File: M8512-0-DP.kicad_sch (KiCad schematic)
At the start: 1 part, among them J1 KL10_6-bay_backplane_connector

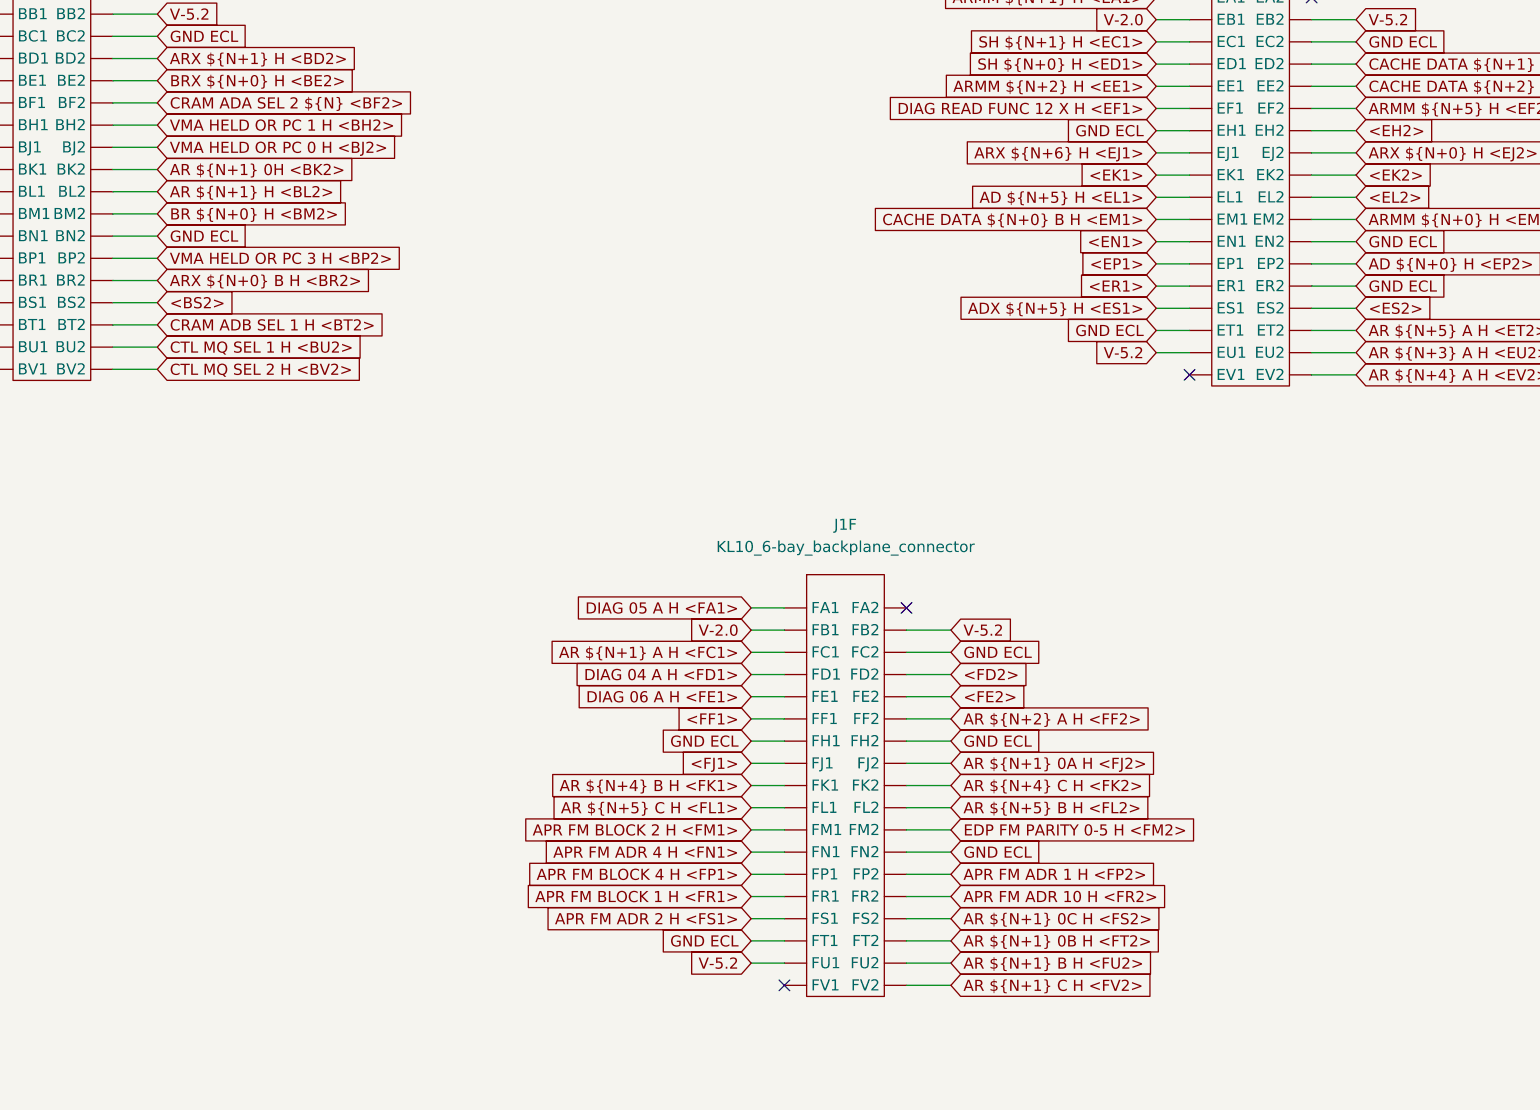
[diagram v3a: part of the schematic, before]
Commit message: Fix a few mislabeld backplane signal names - still more to do
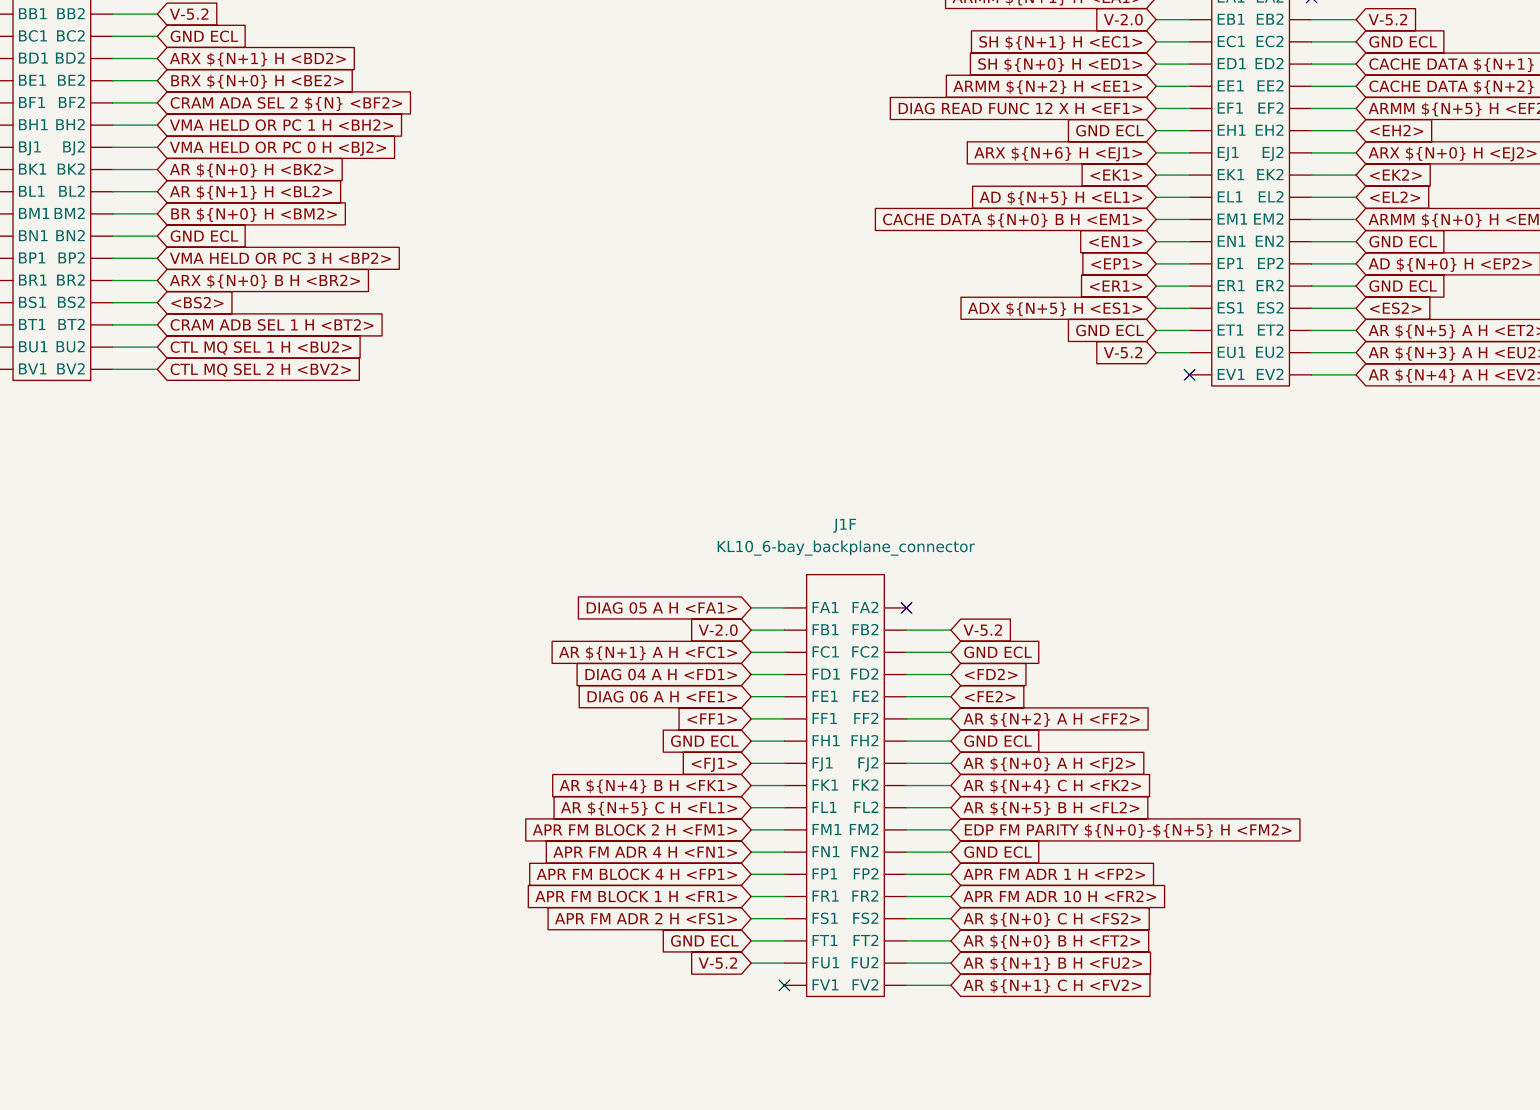
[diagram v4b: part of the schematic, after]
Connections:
- net AR ${N+1} 0A H <FJ2> renamed AR ${N+0} A H <FJ2>
- net AR ${N+1} 0B H <FT2> renamed AR ${N+0} B H <FT2>
- net AR ${N+1} 0C H <FS2> renamed AR ${N+0} C H <FS2>
- net AR ${N+1} 0H <BK2> renamed AR ${N+0} H <BK2>
- net EDP FM PARITY 0-5 H <FM2> renamed EDP FM PARITY ${N+0}-${N+5} H <FM2>
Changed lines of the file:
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@@
     )
   )
-  (global_label "AR ${N+1} 0H <BK2>" (shape input) (at 190.5 128.27 0) (fields_autoplaced)
-    (effects (font (size 1.27 1.27)) (justify left))
-    (property "Intersheet References" "${INTERSHEET_REFS}" (id 0) (at 207.6088 128.1906 0)
+  (global_label "AR ${N+0} H <BK2>" (shape input) (at 190.5 128.27 0) (fields_autoplaced)
+    (effects (font (size 1.27 1.27)) (justify left))
+    (property "Intersheet References" "${INTERSHEET_REFS}" (id 0) (at 213.4145 128.1906 0)
       (effects (font (size 1.27 1.27)) (justify left) hide)
     )
@@
     )
   )
-  (global_label "AR ${N+1} 0B H <FT2>" (shape input) (at 281.305 216.535 0) (fields_autoplaced)
-    (effects (font (size 1.27 1.27)) (justify left))
-    (property "Intersheet References" "${INTERSHEET_REFS}" (id 0) (at 300.1676 216.4556 0)
+  (global_label "AR ${N+0} B H <FT2>" (shape input) (at 281.305 216.535 0) (fields_autoplaced)
+    (effects (font (size 1.27 1.27)) (justify left))
+    (property "Intersheet References" "${INTERSHEET_REFS}" (id 0) (at 305.9733 216.4556 0)
       (effects (font (size 1.27 1.27)) (justify left) hide)
     )
@@
     )
   )
-  (global_label "AR ${N+1} 0C H <FS2>" (shape input) (at 281.305 213.995 0) (fields_autoplaced)
-    (effects (font (size 1.27 1.27)) (justify left))
-    (property "Intersheet References" "${INTERSHEET_REFS}" (id 0) (at 300.4095 213.9156 0)
+  (global_label "AR ${N+0} C H <FS2>" (shape input) (at 281.305 213.995 0) (fields_autoplaced)
+    (effects (font (size 1.27 1.27)) (justify left))
+    (property "Intersheet References" "${INTERSHEET_REFS}" (id 0) (at 306.2152 213.9156 0)
       (effects (font (size 1.27 1.27)) (justify left) hide)
     )
@@
     )
   )
-  (global_label "AR ${N+1} 0A H <FJ2>" (shape input) (at 281.305 196.215 0) (fields_autoplaced)
-    (effects (font (size 1.27 1.27)) (justify left))
-    (property "Intersheet References" "${INTERSHEET_REFS}" (id 0) (at 299.9862 196.1356 0)
+  (global_label "AR ${N+0} A H <FJ2>" (shape input) (at 281.305 196.215 0) (fields_autoplaced)
+    (effects (font (size 1.27 1.27)) (justify left))
+    (property "Intersheet References" "${INTERSHEET_REFS}" (id 0) (at 305.7919 196.1356 0)
       (effects (font (size 1.27 1.27)) (justify left) hide)
     )
@@
     )
   )
-  (global_label "EDP FM PARITY 0-5 H <FM2>" (shape input) (at 281.305 203.835 0) (fields_autoplaced)
-    (effects (font (size 1.27 1.27)) (justify left))
-    (property "Intersheet References" "${INTERSHEET_REFS}" (id 0) (at 313.291 203.7556 0)
-      (effects (font (size 1.27 1.27)) (justify left) hide)
-    )
+  (global_label "EDP FM PARITY ${N+0}-${N+5} H <FM2>" (shape input) (at 281.305 203.835 0) (fields_autoplaced)
+    (effects (font (size 1.27 1.27)) (justify left))
+    (property "Intersheet References" "${INTERSHEET_REFS}" (id 0) (at 324.9024 203.7556 0)
+      (effects (font (size 1.27 1.27)) (justify left) hide)
+    )

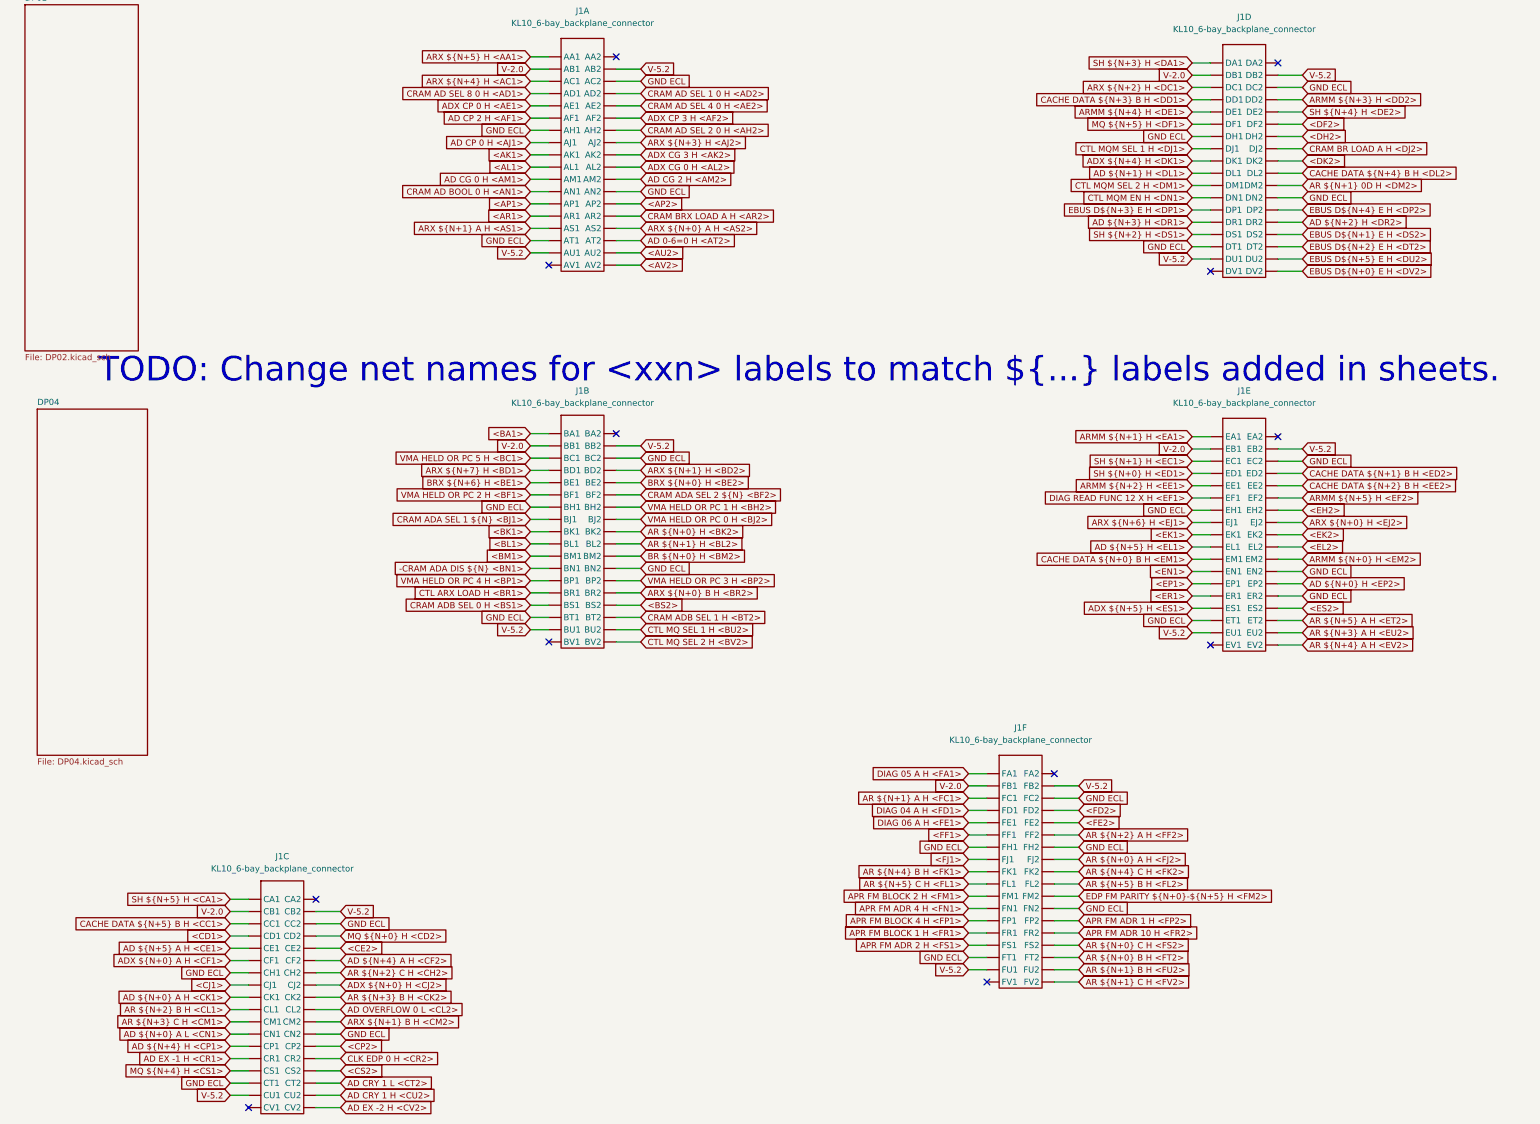
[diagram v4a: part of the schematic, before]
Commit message: Get rid of errors between J1 net name and pages
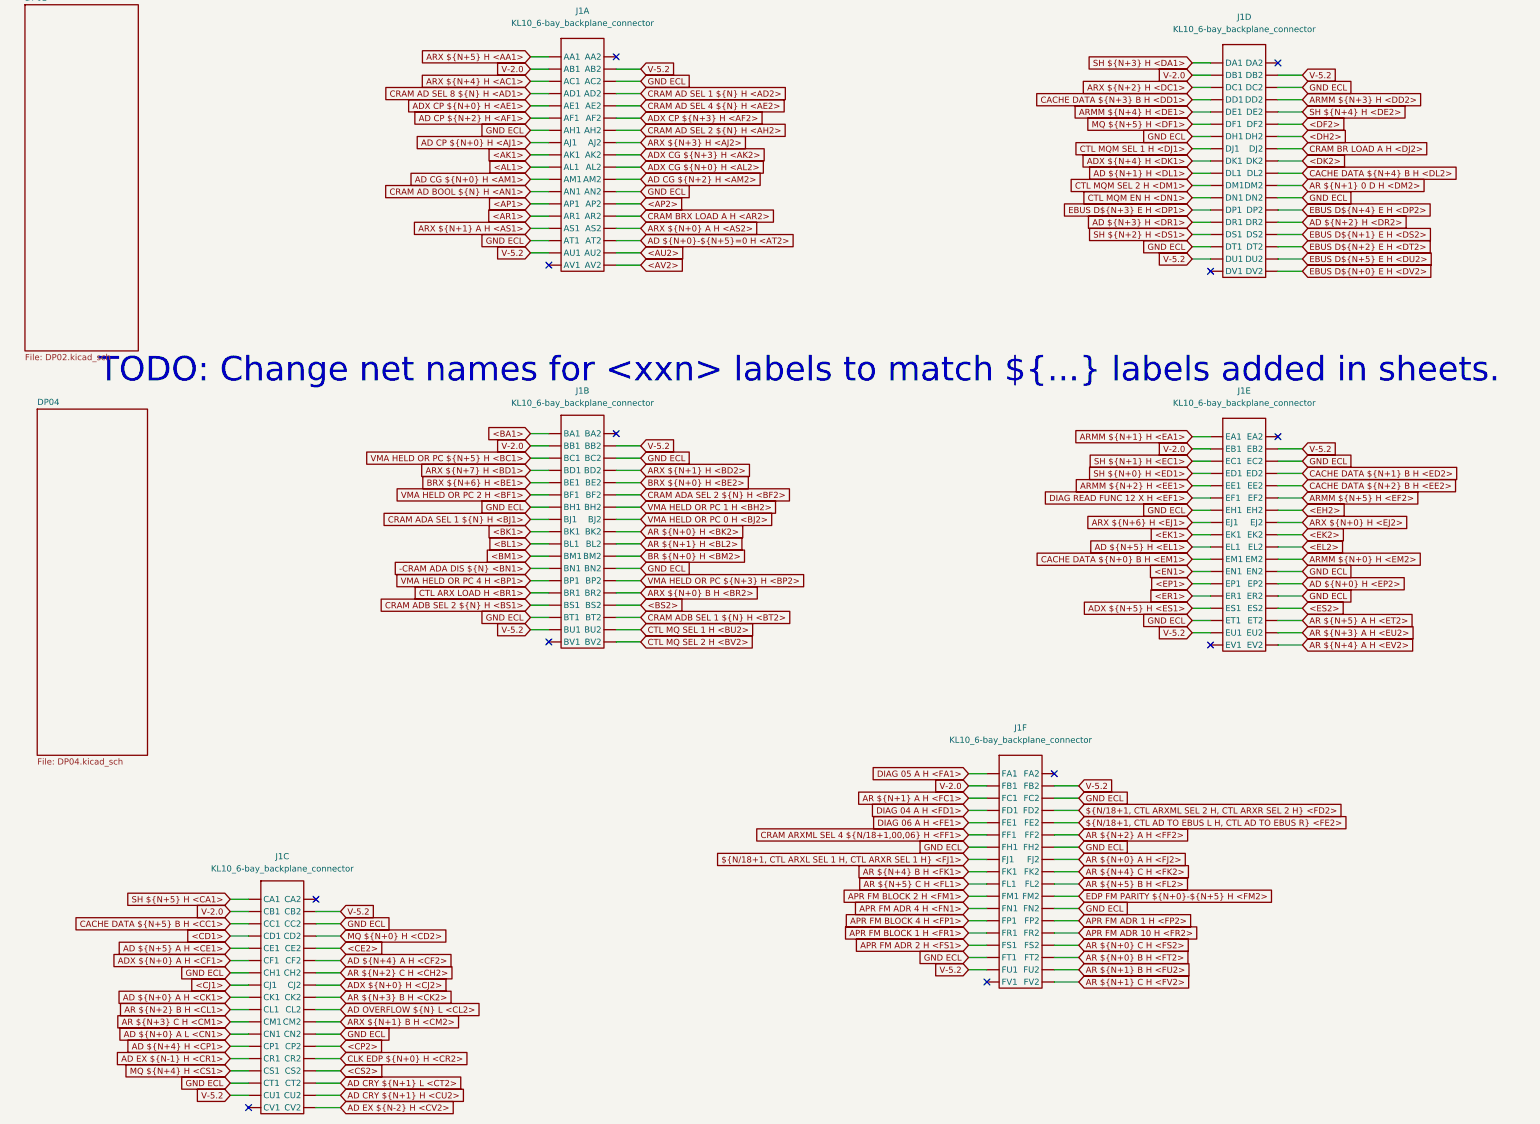
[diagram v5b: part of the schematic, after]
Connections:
- net <FD2> renamed ${N/18+1, CTL ARXML SEL 2 H, CTL ARXR SEL 2 H} <FD2>
- net <FE2> renamed ${N/18+1, CTL AD TO EBUS L H, CTL AD TO EBUS R} <FE2>
- net <FF1> renamed CRAM ARXML SEL 4 ${N/18+1,00,06} H <FF1>
- net <FJ1> renamed ${N/18+1, CTL ARXL SEL 1 H, CTL ARXR SEL 1 H} <FJ1>
- net AD 0-6=0 H <AT2> renamed AD ${N+0}-${N+5}=0 H <AT2>
- net AD CG 0 H <AM1> renamed AD CG ${N+0} H <AM1>
- net AD CG 2 H <AM2> renamed AD CG ${N+2} H <AM2>
- net AD CP 0 H <AJ1> renamed AD CP ${N+0} H <AJ1>
- net AD CP 2 H <AF1> renamed AD CP ${N+2} H <AF1>
- net AD CRY 1 H <CU2> renamed AD CRY ${N+1} H <CU2>
- net AD CRY 1 L <CT2> renamed AD CRY ${N+1} L <CT2>
- net AD EX -1 H <CR1> renamed AD EX ${N-1} H <CR1>
- net AD EX -2 H <CV2> renamed AD EX ${N-2} H <CV2>
- net AD OVERFLOW 0 L <CL2> renamed AD OVERFLOW ${N} L <CL2>
- net ADX CG 0 H <AL2> renamed ADX CG ${N+0} H <AL2>
- net ADX CG 3 H <AK2> renamed ADX CG ${N+3} H <AK2>
- net ADX CP 0 H <AE1> renamed ADX CP ${N+0} H <AE1>
- net ADX CP 3 H <AF2> renamed ADX CP ${N+3} H <AF2>
- net AR ${N+1} 0D H <DM2> renamed AR ${N+1} 0 D H <DM2>
- net CLK EDP 0 H <CR2> renamed CLK EDP ${N+0} H <CR2>
- net CRAM AD BOOL 0 H <AN1> renamed CRAM AD BOOL ${N} H <AN1>
- net CRAM AD SEL 1 0 H <AD2> renamed CRAM AD SEL 1 ${N} H <AD2>
- net CRAM AD SEL 2 0 H <AH2> renamed CRAM AD SEL 2 ${N} H <AH2>
- net CRAM AD SEL 4 0 H <AE2> renamed CRAM AD SEL 4 ${N} H <AE2>
- net CRAM AD SEL 8 0 H <AD1> renamed CRAM AD SEL 8 ${N} H <AD1>
- net CRAM ADA SEL 1 ${N} <BJ1> renamed CRAM ADA SEL 1 ${N} H <BJ1>
- net CRAM ADA SEL 2 ${N} <BF2> renamed CRAM ADA SEL 2 ${N} H <BF2>
- net CRAM ADB SEL 0 H <BS1> renamed CRAM ADB SEL 2 ${N} H <BS1>
- net CRAM ADB SEL 1 H <BT2> renamed CRAM ADB SEL 1 ${N} H <BT2>
- net VMA HELD OR PC 3 H <BP2> renamed VMA HELD OR PC ${N+3} H <BP2>
- net VMA HELD OR PC 5 H <BC1> renamed VMA HELD OR PC ${N+5} H <BC1>

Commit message: Fix up undefined signal names on J1 pins
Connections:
- net <AK1> renamed ${N/30+1, ADX CRY ${N+6} H, CTL ADX CRY 36 H} <AK1>
- net <AL1> renamed ${N/30+1, AD CRY ${N+6} H, AD CRY 36 B H} <AL1>
- net <AP1> renamed # ${N+1} H <AP1>
- net <AP2> renamed # ${N+3} H <AP2>
- net <AR1> renamed # ${N+0} <AR1>
- net <AU2> renamed # ${N+5} H <AU2>
- net <AV2> renamed # ${N+4} H <AV2>
- net <BA1> renamed # ${N+2} H <BA1>
- net <BK1> renamed ${N/30+1, AR ${N+6} H, ARX 00 H} <BK1>
- net <BL1> renamed ${N/30+1, AR ${N+7} h, ARX 01 H} <BL1>
- net <BM1> renamed ${N/30+1 BR ${N+6} A H, BRX 00 H} <BM1>
- net <BS2> renamed ${(N+199)/100, HI, NC} <BS2>
- net <CD1> renamed ${N/30+1, MQ ${N+6} h, AD CRY -02 A H} <CD1>
- net <CE2> renamed ${N/18+1, CON FM WRITE 00-17 L, CON FM WRITE 18-35 L} <CE2>
- net <CJ1> renamed ${N/30+1, ADX ${N+6} H, MQ 00 H} <CJ1>
- net <CP2>: no longer names the net of J1.98 (CP2)
- net <CS2> renamed ${(N+199)/100, ADX 34 H, MQ ${N-2} H} <CS2>
- net <DF2> renamed ${(N+199)/100, ADX 35 H, MQ ${N-1} H} <DF2>
- net <DH2> renamed ${N/6+1, CTL AR 00-08 LOAD L, CTL AR 00-08 LOAD L, CTL AR 09-17 LOAD L, CTL ARR LOAD B L, CTL ARR LOAD B L, CTL ARR LOAD B L} <DH2>
- net <DK2> renamed ${(N+199)/100, AD 34 H, ADX ${N-2} H} <DK2>
- net <EH2> renamed ${N/6+1, CTL AR 00-11 CLR H, CTL AR 00-11 CLR H, CTL AR 12-17 CLR H, CTL ARR CLR H, CTL ARR CLR H, CTL ARR CLR H} <EH2>
- net <EK1> renamed ${N/18+1, CTL ARL SEL 2 H, CTL ARR SEL 2 H} <EK1>
- net <EK2> renamed ${N/6+1, CTL AR 00-08 LOAD L, CTL AR 09-17 LOAD L, CTL AR 09-17 LOAD , CTL ARR LOAD A L, CTL ARR LOAD A L, CTL ARR LOAD A L} <EK2>
- net <EL2> renamed ${N/6+1, AD EX -01 H, AD 05 H, AD 11 H, AD 17 H, AD 23 H, AD 29 H} <EL2>
- net <EN1> renamed ${N/18+1, CTL ARL SEL 1 H, CTL ARR SEL 1 H} <EN1>
- net <EP1> renamed ${N/30+1, AD ${N+6} H, ADX 00 H} <EP1>
- net <ER1> renamed ${N/18+1, CTL ARL SEL 4 H, CRAM ARM SEL 4 A H} <ER1>
- net <ES2> renamed ${(N+199)/100, AD 35 H, AX ${N-1} H} <ES2>
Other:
- note removed: "TODO: Change net names for <xxn> labels to match ${...} labels added in sheets."
- moved on the sheet: J1A, J1B, J1C, J1D, J1E, J1F
